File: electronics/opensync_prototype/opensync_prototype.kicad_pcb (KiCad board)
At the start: 4 copper layers, 160 x 100 mm, 107 parts, among them J1 61400416121, J10 61611042121502, J11 61611042121502, J2 61611042121502, J4 61611042121502, J5 61611042121502, J6 61611042121502, J7 61611042121502, J8 61611042121502, J9 61611042121502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

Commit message: Updated fills
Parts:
- moved H2 5.00 mm to (213.0, 49.0)
- moved H3 5.00 mm to (213.0, 141.0)
- moved C18 3.73 mm to (128.8, 61.2)
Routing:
- net /Power and Data/USB_D-: track 0.00 -> 8.85 mm
- net /Power and Data/USB_D+: track 0.00 -> 8.84 mm
- net Net-(J1-D+): track 0.00 -> 7.05 mm
- net Net-(J1-D-): track 0.00 -> 4.73 mm
- net GND: track 43.2 -> 46.4 mm, vias 59 -> 61
- net Net-(U3-UD-): track 0.00 -> 2.88 mm
- net Net-(U3-UD+): track 0.00 -> 2.87 mm
- net GND_BUS: track 0.00 -> 2.27 mm, vias 0 -> 2
- added copper zone on In1.Cu, net GND_BUS
- added copper zone on F.Cu, net VBUS
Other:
- board size 160 x 100 mm -> 155 x 100 mm

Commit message: Rearranged some stuff
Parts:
- moved C20 1.11 mm to (135.2, 65.2)
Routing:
- net +5V: track 1.17 -> 24.4 mm
- net Net-(U3-PDEN): track 0.00 -> 4.57 mm
- net GND: track 46.4 -> 49.4 mm, vias 61 -> 64
- net GND_BUS: track 2.27 -> 4.58 mm, vias 2 -> 4
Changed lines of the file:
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@@
 		(tags "resistor")
 		(property "Reference" "R26"
-			(at 0 -1.445 90)
+			(at -0.35 -1.345 90)
 			(layer "F.SilkS")
 			(effects
@@
 		(tags "capacitor")
 		(property "Reference" "C18"
-			(at 0 -1.16 0)
+			(at 1.285 -1.2 0)
 			(layer "F.SilkS")
 			(effects
@@
 		(at 130.5 52 180)
 		(property "Reference" "J1"
-			(at 10.4506 -7.5883 0)
+			(at 8.2 -7 0)
 			(layer "F.SilkS")
 			(effects
@@
 	(footprint "RP2350_80QFN_minimal:C_0402_1005Metric_small_pads"
 		(layer "F.Cu")
-		(at 136.31 65.1733 180)
+		(at 135.2 65.1733 180)
 		(descr "Capacitor SMD 0402 (1005 Metric), square (rectangular) end terminal, IPC_7351 nominal, (Body size source: IPC-SM-782 page 76, https://www.pcb-3d.com/wordpress/wp-content/uploads/ipc-sm-782a_amendment_1_and_2.pdf), generated with kicad-footprint-generator")
 		(tags "capacitor")
 		(property "Reference" "C20"
-			(at 0 2.5 0)
+			(at -0.3 1.1733 0)
 			(layer "F.SilkS")
 			(effects
@@
 		(tags "resistor")
 		(property "Reference" "R25"
-			(at 0.15 1.305 270)
+			(at -0.35 1.105 270)
 			(layer "F.SilkS")
 			(effects
@@
 	)
 	(segment
+		(start 161.8775 79)
+		(end 161.8775 77.5225)
+		(width 0.1565)
+		(layer "F.Cu")
+		(net 2)
+	)
+	(segment
 		(start 132.4 103.415)
 		(end 133.115 103.415)
@@
 	)
 	(segment
+		(start 160.03 76)
+		(end 160.8 76)
+		(width 0.1565)
+		(layer "F.Cu")
+		(net 2)
+	)
+	(segment
 		(start 129.6 76.51)
 		(end 129.61 76.5)
@@
 		(net 2)
 	)
+	(segment
+		(start 161.1175 88.8)
+		(end 161.8 88.8)
+		(width 0.1565)
+		(layer "F.Cu")
+		(net 2)
+	)
+	(segment
+		(start 161.8775 77.5225)
+		(end 161.9 77.5)
+		(width 0.5)
+		(layer "F.Cu")
+		(net 2)
+	)
 	(via micro
 		(at 100.2 131.4)
@@
 	)
 	(via micro
+		(at 161.9 77.5)
+		(size 0.6)
+		(drill 0.25)
+		(layers "F.Cu" "In1.Cu")
+		(net 2)
+	)
+	(via micro
 		(at 128.35 105)
 		(size 0.6)
@@
 	)
 	(via micro
+		(at 160.8 76)
+		(size 0.6)
+		(drill 0.25)
+		(layers "F.Cu" "In1.Cu")
+		(net 2)
+	)
+	(via micro
 		(at 121.75 94.4)
 		(size 0.6)
@@
 	)
 	(via micro
+		(at 161.8 88.8)
+		(size 0.6)
+		(drill 0.25)
+		(layers "F.Cu" "In1.Cu")
+		(net 2)
+	)
+	(via micro
 		(at 175.15 131.4)
 		(size 0.6)
@@
 	)
 	(segment
+		(start 137.23 67.2)
+		(end 137.23 65.63)
+		(width 0.1565)
+		(layer "F.Cu")
+		(net 8)
+	)
+	(segment
 		(start 129.6 65.6)
 		(end 129.6 67.19)
@@
 	)
 	(segment
+		(start 135.715 65.1733)
+		(end 136.3733 65.1733)
+		(width 0.1565)
+		(layer "F.Cu")
+		(net 8)
+	)
+	(segment
+		(start 136.3733 65.1733)
+		(end 136.4 65.2)
+		(width 0.5)
+		(layer "F.Cu")
+		(net 8)
+	)
+	(segment
+		(start 137.23 65.63)
+		(end 137.2 65.6)
+		(width 0.5)
+		(layer "F.Cu")
+		(net 8)
+	)
+	(segment
 		(start 129.6 67.19)
 		(end 129.61 67.2)
@@
 	)
 	(via micro
+		(at 137.2 65.6)
+		(size 0.6)
+		(drill 0.25)
+		(layers "F.Cu" "In1.Cu")
+		(free yes)
+		(net 8)
+	)
+	(via micro
 		(at 129.6 65.6)
 		(size 0.6)
@@
 		(net 8)
 	)
+	(via micro
+		(at 136.4 65.2)
+		(size 0.6)
+		(drill 0.25)
+		(layers "F.Cu" "In1.Cu")
+		(free yes)
+		(net 8)
+	)
+	(segment
+		(start 157.2775 79)
+		(end 157.2775 77.4775)
+		(width 0.5)
+		(layer "F.Cu")
+		(net 10)
+	)
+	(segment
+		(start 159 76)
+		(end 158.2 76)
+		(width 0.5)
+		(layer "F.Cu")
+		(net 10)
+	)
+	(segment
+		(start 157 77.2)
+		(end 139.2 77.2)
+		(width 0.5)
+		(layer "F.Cu")
+		(net 10)
+	)
 	(segment
 		(start 99.345 132.36)
@@
 	)
 	(segment
+		(start 139.2 77.2)
+		(end 138.5 76.5)
+		(width 0.5)
+		(layer "F.Cu")
+		(net 10)
+	)
+	(segment
+		(start 157.2775 77.4775)
+		(end 157 77.2)
+		(width 0.5)
+		(layer "F.Cu")
+		(net 10)
+	)
+	(segment
+		(start 158.2 76)
+		(end 157 77.2)
+		(width 0.5)
+		(layer "F.Cu")
+		(net 10)
+	)
+	(segment
 		(start 98.25 132.36)
 		(end 99.345 132.36)
@@
 	)
 	(segment
+		(start 133.42 67.2)
+		(end 135.96 67.2)
+		(width 0.1565)
+		(layer "F.Cu")
+		(net 11)
+	)
+	(segment
+		(start 134.69 67.2)
+		(end 134.69 65.1783)
+		(width 0.1565)
+		(layer "F.Cu")
+		(net 11)
+	)
+	(segment
+		(start 134.69 65.1783)
+		(end 134.685 65.1733)
+		(width 0.5)
+		(layer "F.Cu")
+		(net 11)
+	)
+	(segment
 		(start 131.75 58.74)
 		(end 131.75 58.75)
@@
 		(polygon
 			(pts
-				(xy 120.3995 45) (xy 120.4995 65) (xy 141.4 65) (xy 141.4 45)
+				(xy 120.3995 45) (xy 120.515 68.1) (xy 141.4 68.1) (xy 141.4 45)
 			)
 		)

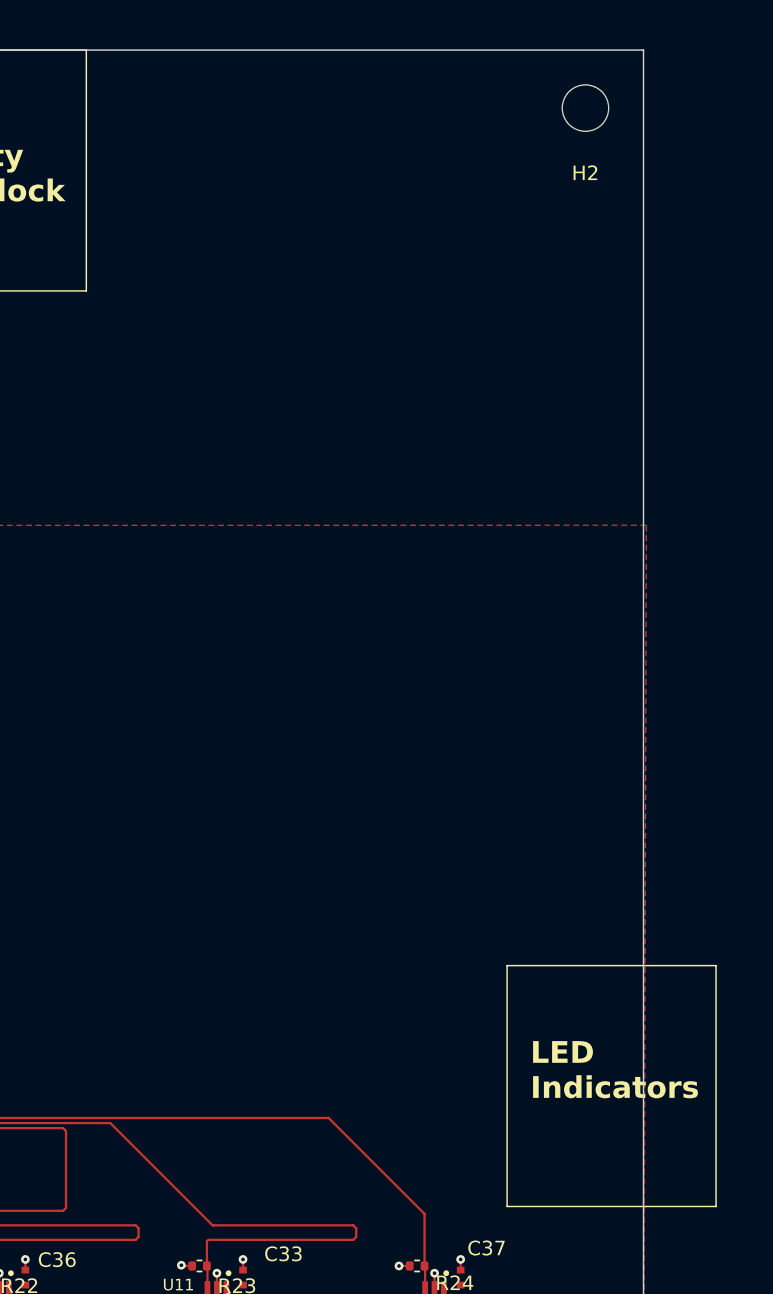
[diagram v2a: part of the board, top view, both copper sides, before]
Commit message: Moved LED indicators
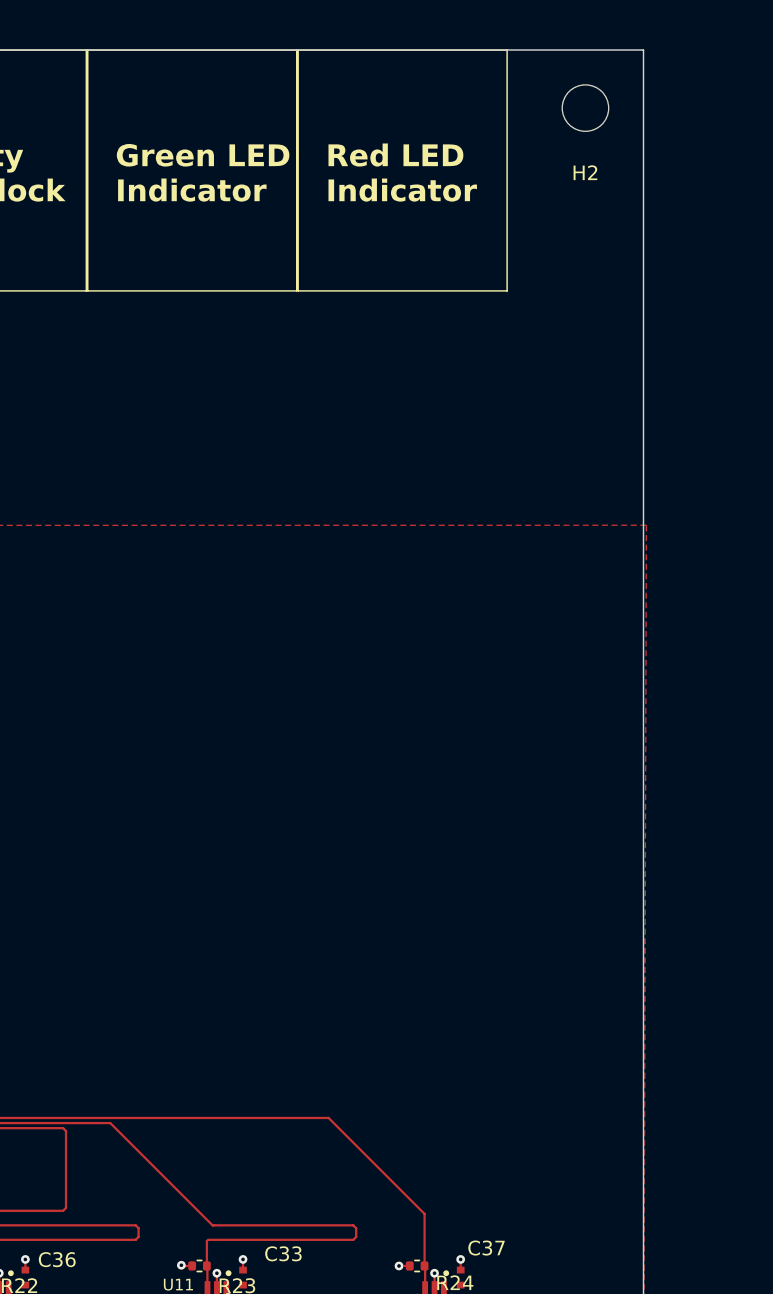
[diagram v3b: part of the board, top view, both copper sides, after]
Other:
- board text added: "Green LED Indicator"
- board text added: "Red LED Indicator"
- board text removed: "LED Indicators"
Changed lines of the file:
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@@
 	)
 	(gr_rect
-		(start 207.6 108.1)
-		(end 222 124.7)
+		(start 178.7 45)
+		(end 193.1 61.6)
+		(stroke
+			(width 0.1)
+			(type solid)
+		)
+		(fill no)
+		(layer "F.SilkS")
+	)
+	(gr_rect
+		(start 193.2 45)
+		(end 207.6 61.6)
 		(stroke
 			(width 0.1)
@@
 		(layer "Edge.Cuts")
 	)
-	(gr_text "LED\nIndicators"
-		(at 209.2 117.4 0)
+	(gr_text "Green LED\nIndicator"
+		(at 180.6 55.6 0)
 		(layer "F.SilkS")
 		(effects
@@
 		)
 	)
+	(gr_text "Red LED\nIndicator"
+		(at 195.1 55.6 0)
+		(layer "F.SilkS")
+		(effects
+			(font
+				(size 1.5 1.5)
+				(thickness 0.3)
+				(bold yes)
+			)
+			(justify left bottom)
+		)
+	)

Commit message: GFround and power plane rework
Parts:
- removed R25, R26: 27, Resistor_SMD:R_0402_1005Metric
- added L2: 15u, RP2350_80QFN_minimal:L_pol_2016, F.Cu at (137.5, 67.8)
- added L3: 22u, RP2350_80QFN_minimal:L_pol_2016, F.Cu at (152.0, 72.9)
- C20: value 100n -> 4.7u
- C22: value 100n -> 10u
- L1: footprint Resistor_SMD:R_0402_1005Metric -> RP2350_80QFN_minimal:L_pol_2016
- U3: value ADUM4160 -> NXE2S0505MC; footprint Package_SO:SOIC-16W_7.5x10.3mm_P1.27mm -> Converter_DCDC:Converter_DCDC_Murata_NXExSxxxxMC_SMD
- moved C22 18.1 mm to (151.9, 71.9), turned to 180 degrees
- moved U3 10.7 mm to (144.7, 70.4), turned to 0 degrees
- moved C19 3.02 mm to (159.9, 73.0)
- moved C21 3.02 mm to (161.0, 85.8)
- moved U1 3.02 mm to (160.0, 79.2)
- moved C20 2.75 mm to (137.5, 66.7)
- moved J10 1.00 mm to (187.0, 139.0)
- moved J11 1.00 mm to (202.0, 139.0)
- moved J2 1.00 mm to (77.0, 139.0)
- moved J4 1.00 mm to (97.0, 139.0)
- moved J5 1.00 mm to (112.0, 139.0)
- moved J6 1.00 mm to (127.0, 139.0)
- moved J7 1.00 mm to (142.0, 139.0)
- moved J8 1.00 mm to (157.0, 139.0)
- moved J9 1.00 mm to (172.0, 139.0)
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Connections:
- net Net-(U2-VREG_LX) renamed /Microcontroller and Ext. Clock/VREG_LX
- C20 pad 2: Net-(U3-PDEN) -> VBUS
- C22 pad 1: Net-(U3-PIN) -> +5V
- J1 pad 2: Net-(J1-D-) -> /Power and Data/USB_D-
- J1 pad 3: Net-(J1-D+) -> /Power and Data/USB_D+
- U3 pad 1: VBUS -> GND_BUS
- U3 pad 14: Net-(U3-PIN) -> unconnected-(U3-NC-Pad14)
- U3 pad 3: Net-(U3-PDEN) -> Net-(U3-+VIN)
- U3 pad 7: Net-(U3-UD+) -> GND
- U3 pad 8: GND_BUS -> Net-(U3-+VOUT)
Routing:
- net +5V: track 24.4 -> 1.17 mm
- net /Power and Data/USB_D+: track 8.84 -> 29.1 mm
- net /Power and Data/USB_D-: track 8.85 -> 27.1 mm
- net Net-(J1-D+): track 7.05 -> 0.00 mm
- net Net-(J1-D-): track 4.73 -> 0.00 mm
- net Net-(U3-PDEN): track 4.57 -> 0.00 mm
- net Net-(U3-UD-): track 2.88 -> 0.00 mm
- net Net-(U3-UD+): track 2.87 -> 0.00 mm
- net GND: track 49.4 -> 47.0 mm, vias 64 -> 62
- net Net-(U3-+VIN): track 0.00 -> 2.06 mm
- net GND_BUS: track 4.58 -> 3.09 mm, vias 4 -> 3
- net VBUS: track 0.00 -> 1.12 mm
- net Net-(U5-B): track 4.65 -> 3.69 mm
- net Net-(U9-B): track 4.65 -> 3.70 mm
- net Net-(U8-B): track 4.65 -> 3.70 mm
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- added copper zone on F.Cu, net /Microcontroller and Ext. Clock/VREG_LX
- removed copper zone on F.Cu, net /VREG_LX
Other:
- board text removed: "USB Isolation"

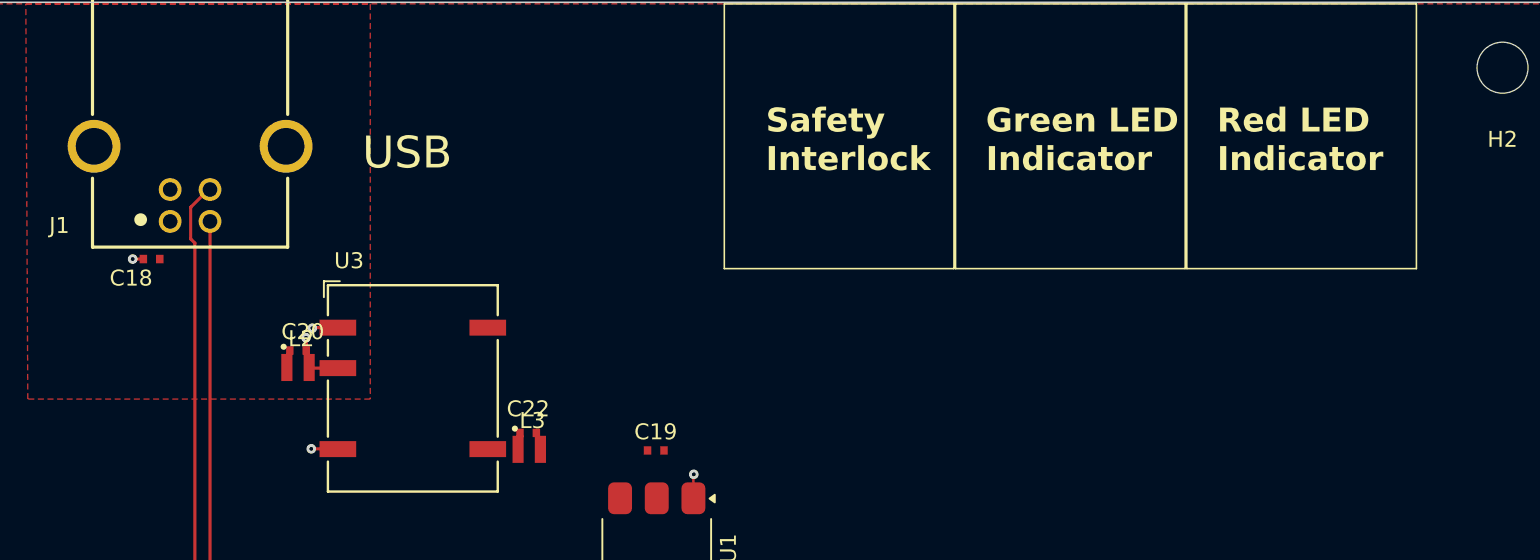
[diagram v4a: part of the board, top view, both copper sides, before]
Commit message: Fixed RF jack problems and LED sketch
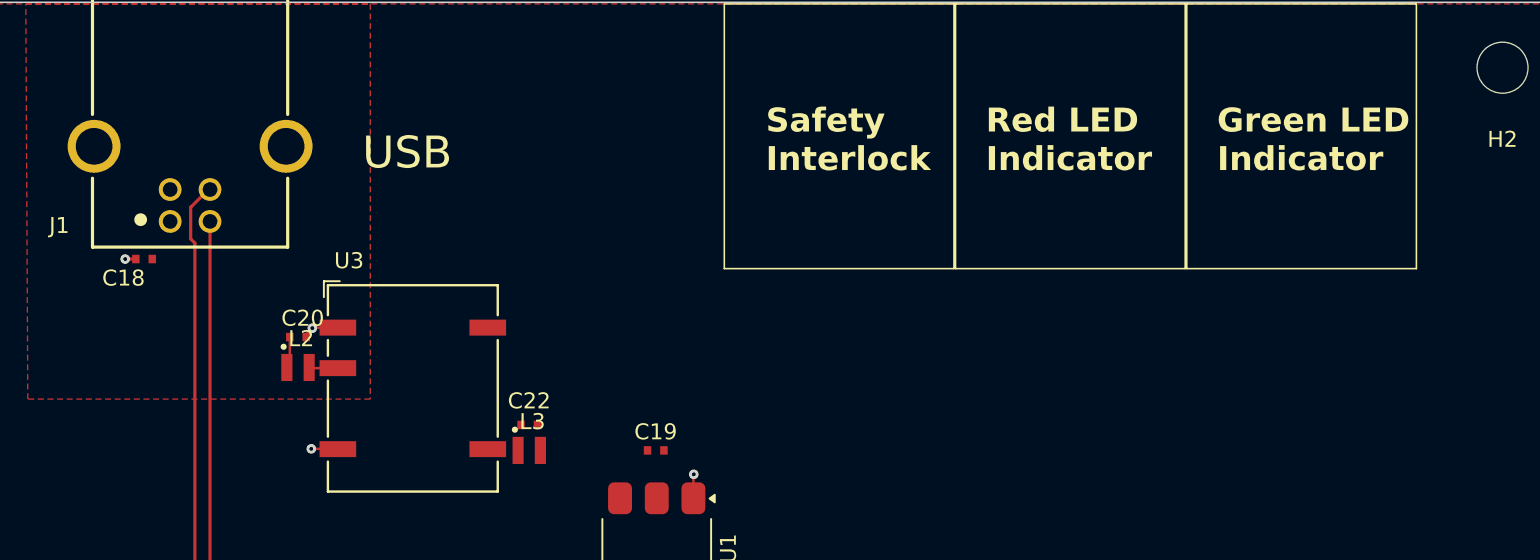
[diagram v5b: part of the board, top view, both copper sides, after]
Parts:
- moved C20 0.84 mm to (137.5, 65.9)
- moved C22 0.50 mm to (152.0, 71.4)
- moved C18 0.47 mm to (127.8, 61.0)
- moved L3 0.07 mm to (152.0, 73.0)
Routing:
- net VBUS: track 1.12 -> 2.03 mm
- net GND_BUS: track 3.09 -> 3.02 mm, vias 3 -> 2

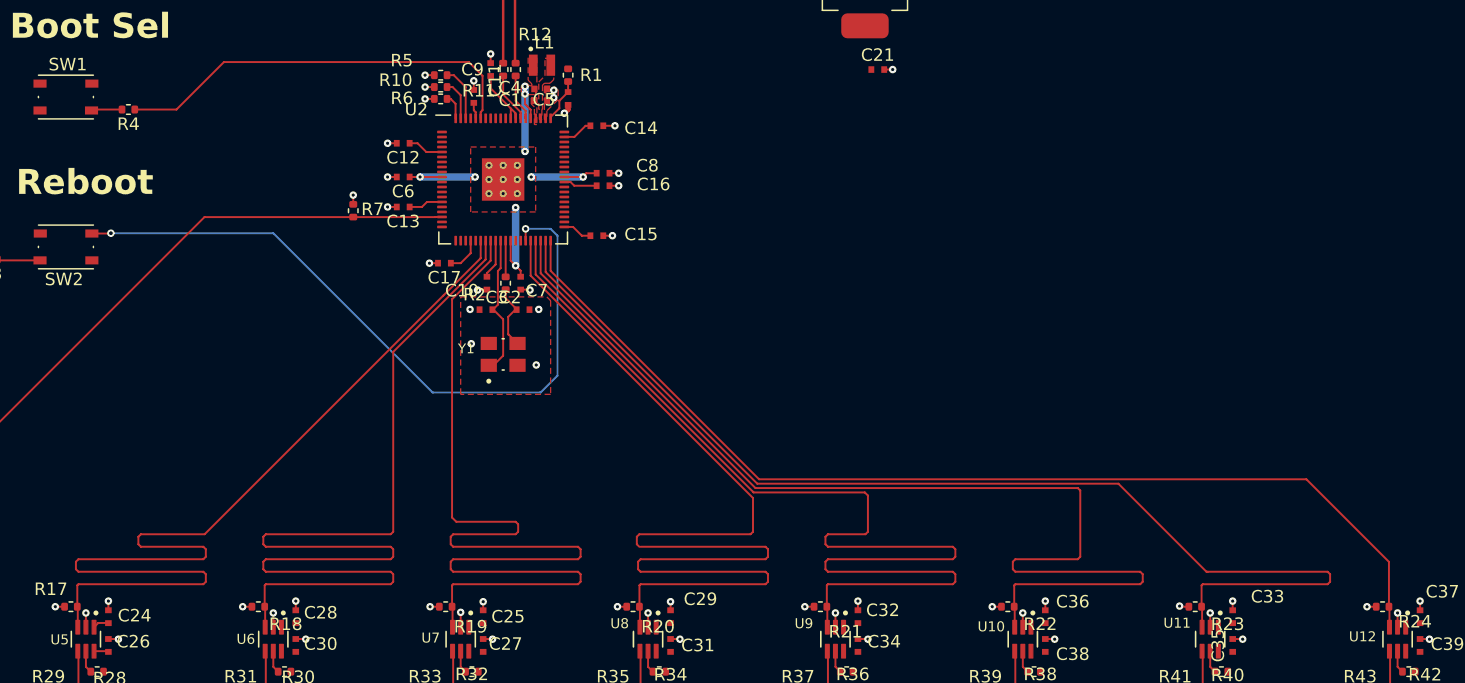
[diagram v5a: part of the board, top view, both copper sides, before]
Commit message: Increased spacing for output traces
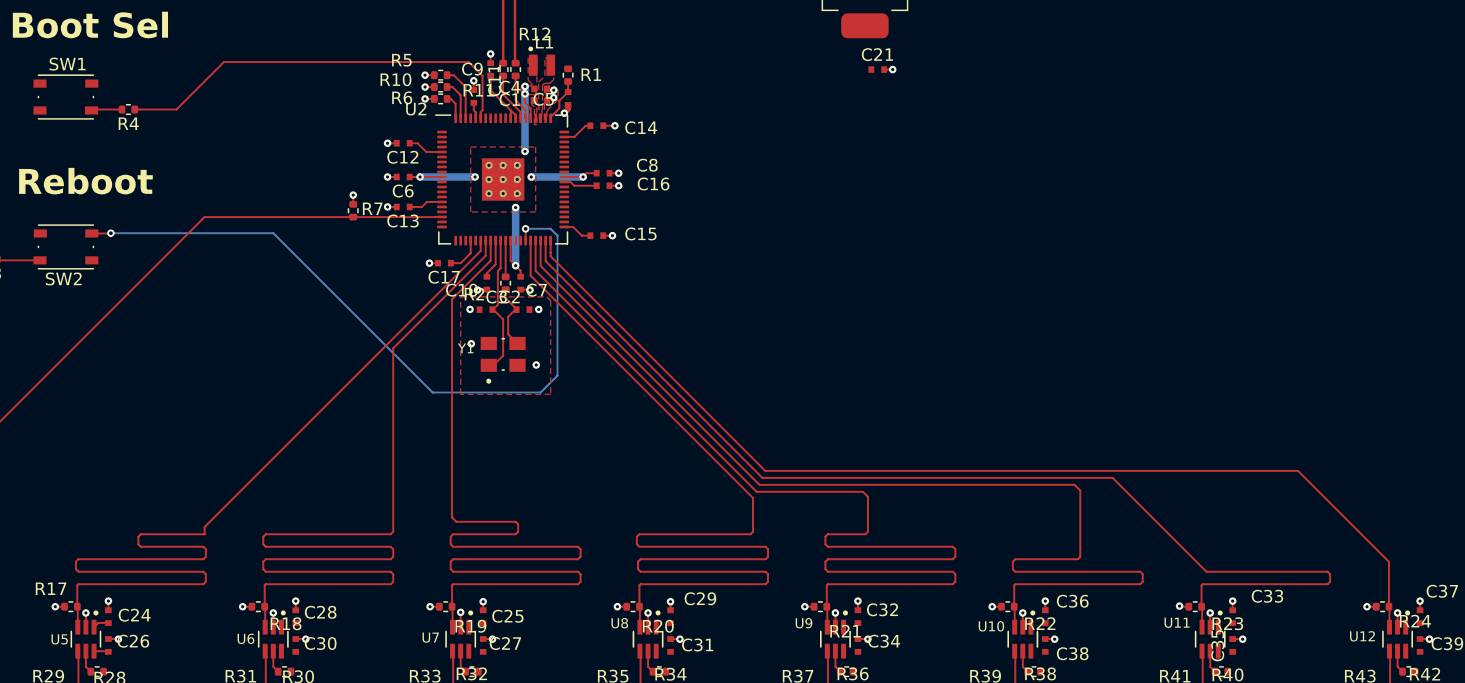
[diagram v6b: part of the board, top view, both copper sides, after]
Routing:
- net /Microcontroller and Ext. Clock/OUTPUT_8: track 84.4 -> 83.7 mm
- net /Microcontroller and Ext. Clock/OUTPUT_7: track 89.7 -> 89.2 mm
